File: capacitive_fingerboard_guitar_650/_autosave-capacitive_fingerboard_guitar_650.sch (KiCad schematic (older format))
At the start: 138 parts, among them J1 Conn_01x08, J11 Conn_02x04_Top_Bottom, J12 Conn_02x04_Top_Bottom, J14 Conn_02x04_Top_Bottom, J15 Conn_02x04_Top_Bottom, J17 Conn_02x04_Top_Bottom, J18 Conn_02x04_Top_Bottom, J2 Conn_02x04_Top_Bottom, J3 Conn_02x04_Top_Bottom, J5 Conn_02x04_Top_Bottom, J6 Conn_02x04_Top_Bottom, J8 Conn_02x04_Top_Bottom, J9 Conn_02x04_Top_Bottom, U1 Electrode, U10 Electrode, U100 Electrode, U101 Electrode, U102 Electrode, U103 Electrode, U104 Electrode, U105 Electrode, U106 Electrode, U107 Electrode, U108 Electrode, U109 Electrode, U11 Electrode, U110 Electrode, U111 Electrode, U112 Electrode, U113 Electrode, U114 Electrode, U115 Electrode, U116 Electrode, U117 Electrode, U118 Electrode, U119 Electrode, U12 Electrode, U120 Electrode, U13 Electrode, U14 Electrode, U15 Electrode, U16 Electrode, U17 Electrode, U18 Electrode, U19 Electrode, U2 Electrode, U20 Electrode, U21 Electrode, U22 Electrode, U23 Electrode, U24 Electrode, U25 Electrode, U26 Electrode, U27 Electrode, U28 Electrode, U29 Electrode, U3 Electrode, U30 Electrode, U31 Electrode, U32 Electrode, U33 Electrode, U34 Electrode, U35 Electrode, U36 Electrode, U37 Electrode, U38 Electrode, U39 Electrode, U4 Electrode, U40 Electrode, U41 Electrode, U42 Electrode, U43 Electrode, U44 Electrode, U45 Electrode, U46 Electrode, U47 Electrode, U48 Electrode, U49 Electrode, U5 Electrode, U50 Electrode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

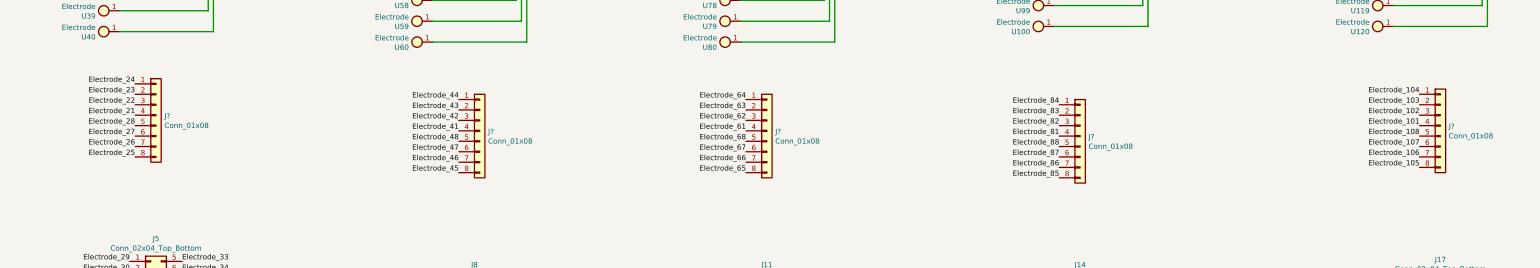
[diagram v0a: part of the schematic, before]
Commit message: Added traces for the first third
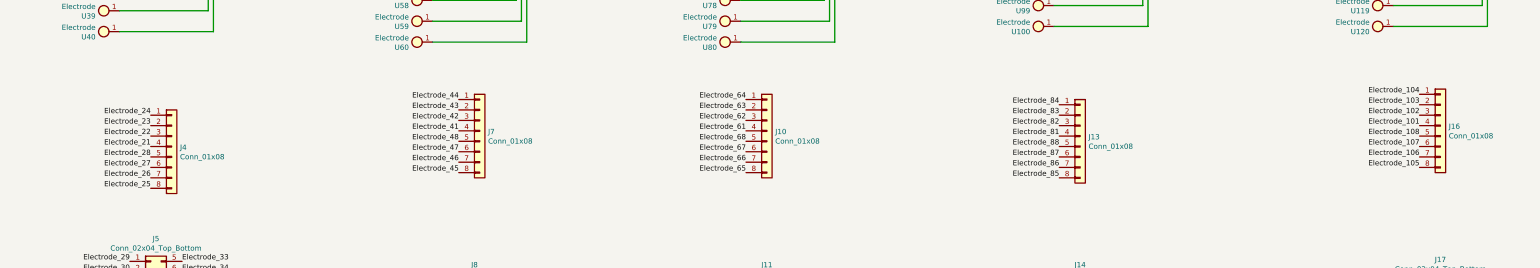
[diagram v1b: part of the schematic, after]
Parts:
- gave numbers to parts that had none: 5
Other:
- moved on the sheet: J4
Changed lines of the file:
@@
 Text Label 1650 7950 2    50   ~ 0
 Electrode_20
-Text Label 6100 5750 2    50   ~ 0
+Text Label 6250 6050 2    50   ~ 0
 Electrode_21
-Text Label 6100 5650 2    50   ~ 0
+Text Label 6250 5950 2    50   ~ 0
 Electrode_22
-Text Label 6100 5550 2    50   ~ 0
+Text Label 6250 5850 2    50   ~ 0
 Electrode_23
-Text Label 6100 5450 2    50   ~ 0
+Text Label 6250 5750 2    50   ~ 0
 Electrode_24
-Text Label 6100 6150 2    50   ~ 0
+Text Label 6250 6450 2    50   ~ 0
 Electrode_25
-Text Label 6100 6050 2    50   ~ 0
+Text Label 6250 6350 2    50   ~ 0
 Electrode_26
-Text Label 6100 5950 2    50   ~ 0
+Text Label 6250 6250 2    50   ~ 0
 Electrode_27
-Text Label 6100 5850 2    50   ~ 0
+Text Label 6250 6150 2    50   ~ 0
 Electrode_28
 Text Label 6050 7150 2    50   ~ 0
@@
 $EndComp
 $Comp
-L Connector_Generic:Conn_01x08 J?
+L Connector_Generic:Conn_01x08 J4
 U 1 1 67821A9F
-P 6300 5750
-F 0 "J?" H 6380 5742 50  0000 L CNN
-F 1 "Conn_01x08" H 6380 5651 50  0000 L CNN
-F 2 "Custom:SAMTEC_TSM-108-01-F-SV" H 6300 5750 50  0001 C CNN
-F 3 "~" H 6300 5750 50  0001 C CNN
-	1    6300 5750
-	1    0    0    -1
-$EndComp
-$Comp
-L Connector_Generic:Conn_01x08 J?
+P 6450 6050
+F 0 "J4" H 6530 6042 50  0000 L CNN
+F 1 "Conn_01x08" H 6530 5951 50  0000 L CNN
+F 2 "Custom:SAMTEC_TSM-108-01-F-SV" H 6450 6050 50  0001 C CNN
+F 3 "~" H 6450 6050 50  0001 C CNN
+	1    6450 6050
+	1    0    0    -1
+$EndComp
+$Comp
+L Connector_Generic:Conn_01x08 J7
 U 1 1 678646F7
 P 9400 5900
-F 0 "J?" H 9480 5892 50  0000 L CNN
+F 0 "J7" H 9480 5892 50  0000 L CNN
 F 1 "Conn_01x08" H 9480 5801 50  0000 L CNN
 F 2 "Custom:SAMTEC_TSM-108-01-F-SV" H 9400 5900 50  0001 C CNN
@@
 $EndComp
 $Comp
-L Connector_Generic:Conn_01x08 J?
+L Connector_Generic:Conn_01x08 J10
 U 1 1 6786580B
 P 12150 5900
-F 0 "J?" H 12230 5892 50  0000 L CNN
+F 0 "J10" H 12230 5892 50  0000 L CNN
 F 1 "Conn_01x08" H 12230 5801 50  0000 L CNN
 F 2 "Custom:SAMTEC_TSM-108-01-F-SV" H 12150 5900 50  0001 C CNN
@@
 $EndComp
 $Comp
-L Connector_Generic:Conn_01x08 J?
+L Connector_Generic:Conn_01x08 J13
 U 1 1 67865E8D
 P 15150 5950
-F 0 "J?" H 15230 5942 50  0000 L CNN
+F 0 "J13" H 15230 5942 50  0000 L CNN
 F 1 "Conn_01x08" H 15230 5851 50  0000 L CNN
 F 2 "Custom:SAMTEC_TSM-108-01-F-SV" H 15150 5950 50  0001 C CNN
@@
 $EndComp
 $Comp
-L Connector_Generic:Conn_01x08 J?
+L Connector_Generic:Conn_01x08 J16
 U 1 1 67866B5E
 P 18600 5850
-F 0 "J?" H 18680 5842 50  0000 L CNN
+F 0 "J16" H 18680 5842 50  0000 L CNN
 F 1 "Conn_01x08" H 18680 5751 50  0000 L CNN
 F 2 "Custom:SAMTEC_TSM-108-01-F-SV" H 18600 5850 50  0001 C CNN
